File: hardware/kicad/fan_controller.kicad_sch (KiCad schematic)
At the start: 84 parts, among them J1 12V IN, J10 AIN2, J11 AIN3, J12 AIN4, J13 AIN5, J14 AIN6, J2 BluePill A, J3 BluePill B, J4 USB int, J5 FAN1, J6 FAN2, J7 FAN3, J8 FAN4, J9 AIN1, Q1 BSS138, Q2 BSS138, Q3 BSS138, Q4 BSS138, U1 USBLC6-2SC6

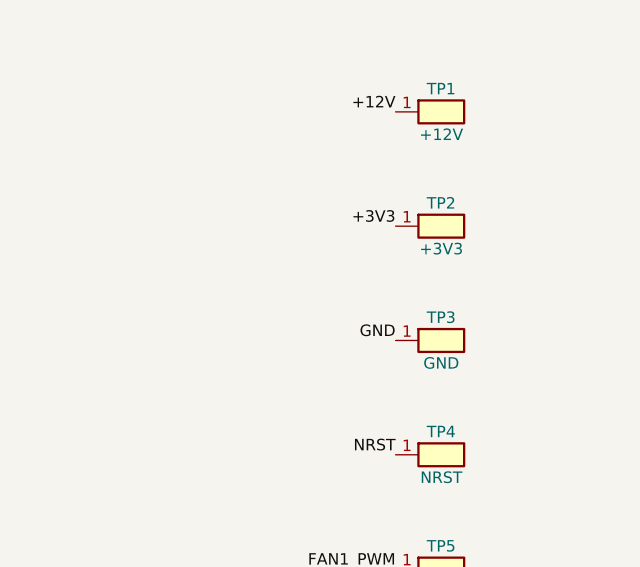
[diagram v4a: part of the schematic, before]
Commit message: hw: route 21 missing nets, remove 3V3/GND test point pair
21 nets (mostly BluePill header J2/J3 to main-board parts) were
never actually routed, despite earlier DRC checks reporting zero
errors - the MCP DRC wrapper used doesn't run KiCad's unconnected-
items check. Verified with native kicad-cli --severity-all.

Routed via Freerouting (autoroute, best-of-3), then manually closed
the 2 nets it couldn't finish (GND, +3V3A) and fixed a short the
autorouted +3V3A trace made against an existing GND track, plus a
board-edge clearance violation on FAN3_TACH.

Also removed TP2 (+3V3) / TP3 (GND), a probe pair that served no
circuit function, plus their stub traces.

Native kicad-cli DRC (10.0.7): 0 errors, 0 unconnected items.

Signed-off-by: Roman Skakun <rm.skakun@gmail.com>
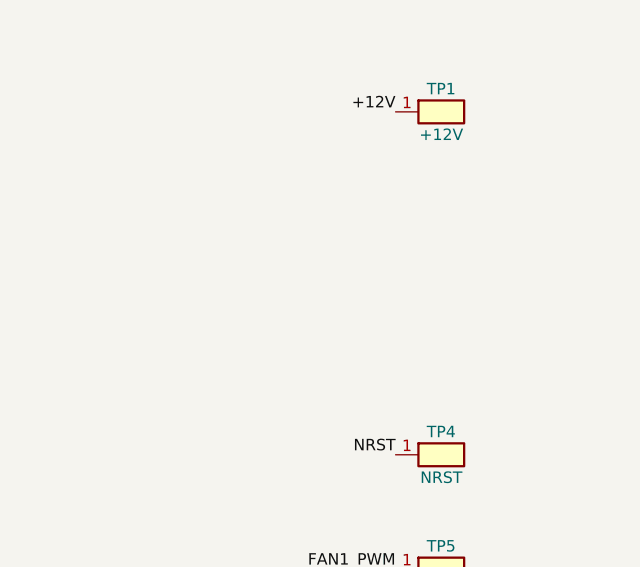
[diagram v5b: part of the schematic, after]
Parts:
- removed TP2: +3V3, TestPoint:TestPoint_Pad_D1.5mm, symbol fanctl:TestPoint
- removed TP3: GND, TestPoint:TestPoint_Pad_D1.5mm, symbol fanctl:TestPoint
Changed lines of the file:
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@@
 		)
 	)
-	(label "+3V3"
-		(at 736.6 58.42 180)
-		(effects
-			(font
-				(size 1.27 1.27)
-			)
-			(justify right bottom)
-		)
-	)
 	(label "GND"
 		(at 200.66 54.61 180)
@@
 		)
 	)
-	(label "GND"
-		(at 736.6 71.12 180)
-		(effects
-			(font
-				(size 1.27 1.27)
-			)
-			(justify right bottom)
-		)
-	)
 	(label "+5V"
 		(at 109.22 148.59 180)
@@
 	)
 	(symbol
-		(lib_id "fanctl:TestPoint")
-		(at 741.68 71.12 0)
-		(unit 1)
-		(body_style 1)
-		(exclude_from_sim no)
-		(in_bom yes)
-		(on_board yes)
-		(in_pos_files yes)
-		(dnp no)
-		(property "Reference" "TP3"
-			(at 741.68 68.58 0)
-			(show_name no)
-			(do_not_autoplace no)
-			(effects
-				(font
-					(size 1.27 1.27)
-				)
-			)
-		)
-		(property "Value" "GND"
-			(at 741.68 73.66 0)
-			(show_name no)
-			(do_not_autoplace no)
-			(effects
-				(font
-					(size 1.27 1.27)
-				)
-			)
-		)
-		(property "Footprint" "TestPoint:TestPoint_Pad_D1.5mm"
-			(at 741.68 71.12 0)
-			(hide yes)
-			(show_name no)
-			(do_not_autoplace no)
-			(effects
-				(font
-					(size 1.27 1.27)
-				)
-			)
-		)
-		(property "Datasheet" ""
-			(at 741.68 71.12 0)
-			(hide yes)
-			(show_name no)
-			(do_not_autoplace no)
-			(effects
-				(font
-					(size 1.27 1.27)
-				)
-			)
-		)
-		(property "Description" "Probe pad"
-			(at 741.68 71.12 0)
-			(hide yes)
-			(show_name no)
-			(do_not_autoplace no)
-			(effects
-				(font
-					(size 1.27 1.27)
-				)
-			)
-		)
-		(property "MPN" ""
-			(at 741.68 71.12 0)
-			(hide yes)
-			(show_name no)
-			(do_not_autoplace no)
-			(effects
-				(font
-					(size 1.27 1.27)
-				)
-			)
-		)
-		(pin "1"
-		)
-		(instances
-			(project "fan_controller"
-				(path "/70b8c4ee-a575-5d0b-ad3b-d6e1fd85f7ba"
-					(reference "TP3")
-					(unit 1)
-				)
-			)
-		)
-	)
-	(symbol
 		(lib_id "fanctl:Polyfuse")
 		(at 30.48 60.96 0)
@@
 					(unit 1)
 				)
-			)
-		)
-	)
-	(symbol
-		(lib_id "fanctl:TestPoint")
-		(at 741.68 58.42 0)
-		(unit 1)
-		(body_style 1)
-		(exclude_from_sim no)
-		(in_bom yes)
-		(on_board yes)
-		(in_pos_files yes)
-		(dnp no)
-		(property "Reference" "TP2"
-			(at 741.68 55.88 0)
-			(show_name no)
-			(do_not_autoplace no)
-			(effects
-				(font
-					(size 1.27 1.27)
-				)
-			)
-		)
-		(property "Value" "+3V3"
-			(at 741.68 60.96 0)
-			(show_name no)
-			(do_not_autoplace no)
-			(effects
-				(font
-					(size 1.27 1.27)
-				)
-			)
-		)
-		(property "Footprint" "TestPoint:TestPoint_Pad_D1.5mm"
-			(at 741.68 58.42 0)
-			(hide yes)
-			(show_name no)
-			(do_not_autoplace no)
-			(effects
-				(font
-					(size 1.27 1.27)
-				)
-			)
-		)
-		(property "Datasheet" ""
-			(at 741.68 58.42 0)
-			(hide yes)
-			(show_name no)
-			(do_not_autoplace no)
-			(effects
-				(font
-					(size 1.27 1.27)
-				)
-			)
-		)
-		(property "Description" "Probe pad"
-			(at 741.68 58.42 0)
-			(hide yes)
-			(show_name no)
-			(do_not_autoplace no)
-			(effects
-				(font
-					(size 1.27 1.27)
-				)
-			)
-		)
-		(property "MPN" ""
-			(at 741.68 58.42 0)
-			(hide yes)
-			(show_name no)
-			(do_not_autoplace no)
-			(effects
-				(font
-					(size 1.27 1.27)
-				)
-			)
-		)
-		(pin "1"
-		)
-		(instances
-			(project "fan_controller"
-				(path "/70b8c4ee-a575-5d0b-ad3b-d6e1fd85f7ba"
-					(reference "TP2")
-					(unit 1)
-				)

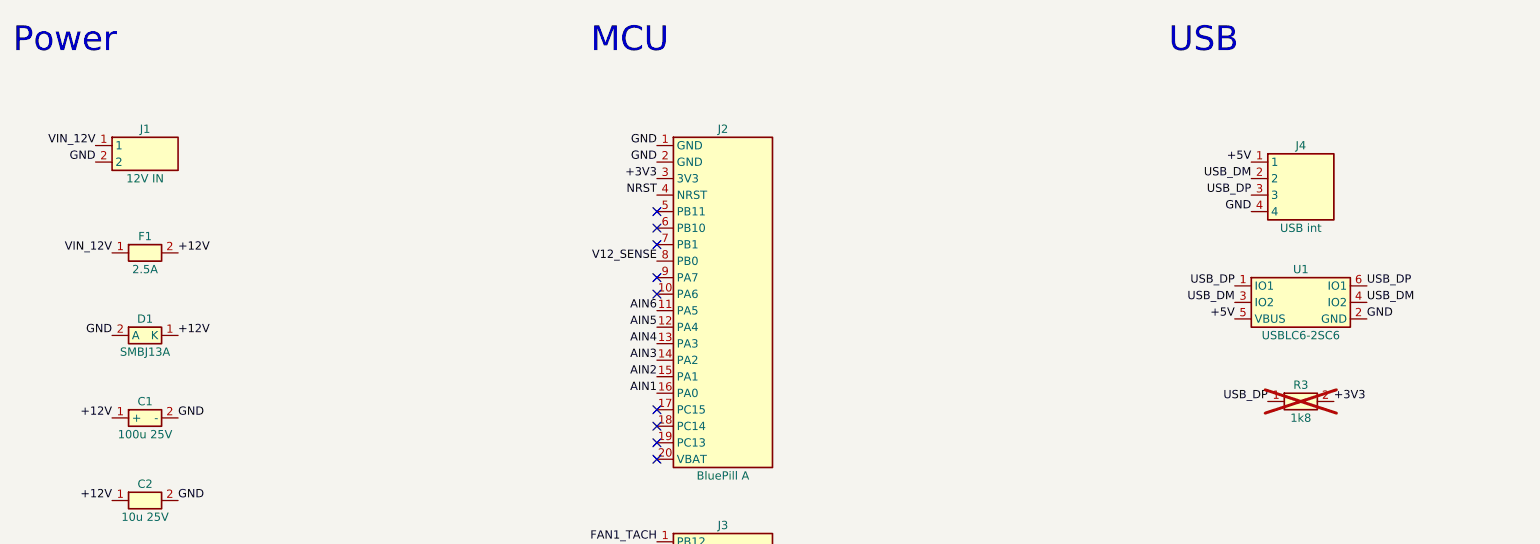
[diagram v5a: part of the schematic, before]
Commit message: hw: swap 12V connector to Mate-N-Lok, drop main-board USB, rotate J3
Replace J1 (2-pin Phoenix screw terminal) with TE Connectivity
350424-1, a 4-circuit Mate-N-Lok PCB header (2x GND + 2x VIN_12V,
12A/250V per pin, 0.2in pitch). Custom footprint built from the
part's real datasheet drawing (drill/pitch), registered as a
project-local fanctl.pretty library since no footprint libraries
are installed in this environment.

Remove the main-board USB path entirely (J4 header, U1 ESD chip,
R3 pullup): the Blue Pill module's own USB port covers this, so
routing USB_DP/USB_DM across the main board was unnecessary. This
also freed board area.

Rotate J3 (Blue Pill B header) 180 degrees in place, and relocate
the 12V input protection cluster (F1 fuse, D1 TVS, C1 bulk cap,
C2 10u cap, FB1 ferrite) into the space freed by the USB removal,
to fit the physically larger J1 connector without colliding with
J3's courtyard.

KNOWN INCOMPLETE: native kicad-cli --severity-all DRC currently
reports 5 unconnected items, 7 shorts, and 3 track crossings,
all localized to the relocated F1/D1/C1/C2/FB1 cluster and nearby
NRST routing. Needs one more Freerouting pass on +12V/GND/NRST/
+3V3A plus manual cleanup before this is fab-ready. gen_kicad.py
(the board's generator script / BOM source of truth) has not yet
been updated to match these changes.

Signed-off-by: Roman Skakun <rm.skakun@gmail.com>
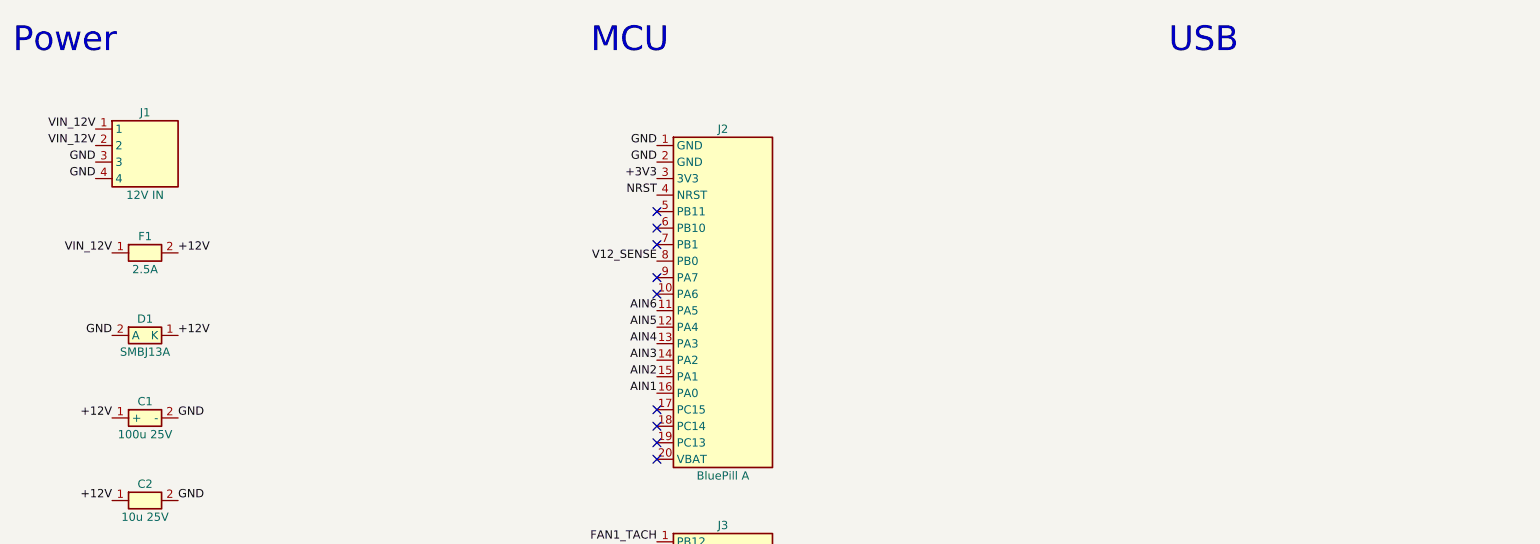
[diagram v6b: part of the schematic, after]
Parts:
- removed J1: 12V IN, TerminalBlock_Phoenix:TerminalBlock_Phoenix_MKDS-1,5-2-5.08_1x02_P5.08mm_Horizontal, symbol fanctl:Conn_01x02
- removed J4: USB int, Connector_PinHeader_2.54mm:PinHeader_1x04_P2.54mm_Vertical, symbol fanctl:Conn_01x04
- removed R3: 1k8, Resistor_SMD:R_0603_1608Metric, symbol fanctl:R
- removed U1: USBLC6-2SC6, Package_TO_SOT_SMD:SOT-23-6, symbol fanctl:USBLC6-2SC6
- added J1: 12V IN, fanctl:ConnHeader_MateNLok_1x04_P5.08mm_Vertical, symbol fanctl:Conn_01x04
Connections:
- net GND: now also J1.3, J1.4
- net VIN_12V: now also J1.1, J1.2

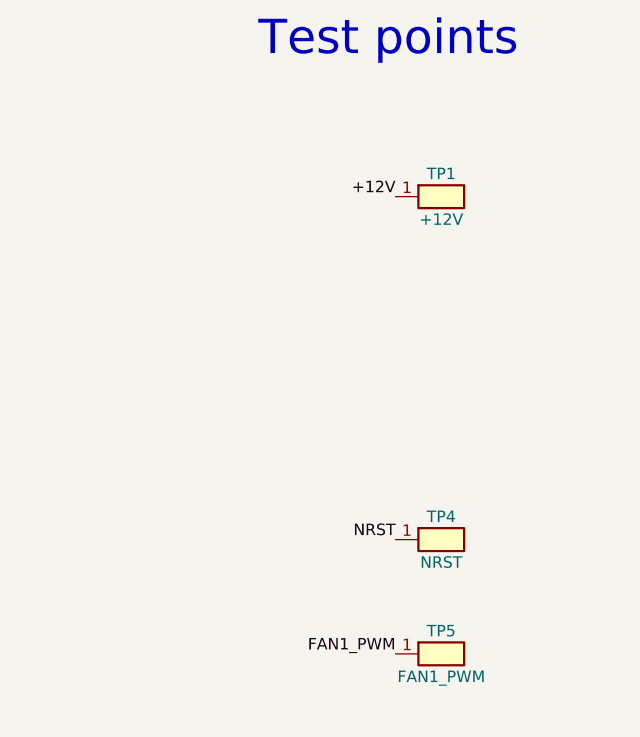
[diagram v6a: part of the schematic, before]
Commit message: hw: sync schematic to board after removing TP1/TP4 test points
Board no longer carries TP1 (+12V probe) and TP4 (NRST probe); remove
the matching symbols and their orphaned net labels from the schematic
so both files agree. Cross-checked all 77 references: footprints and
values now match exactly between schematic and board.

ERC: 0 errors, 4 warnings (pre-existing single-pin-label style,
consistent with the rest of the sheet).

Signed-off-by: Roman Skakun <rm.skakun@gmail.com>
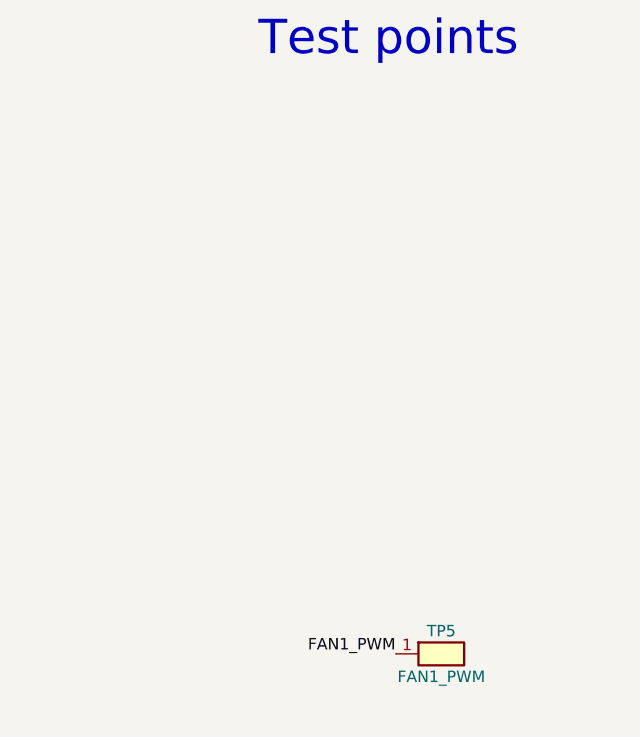
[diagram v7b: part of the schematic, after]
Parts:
- removed TP1: +12V, TestPoint:TestPoint_Pad_D1.5mm, symbol fanctl:TestPoint
- removed TP4: NRST, TestPoint:TestPoint_Pad_D1.5mm, symbol fanctl:TestPoint
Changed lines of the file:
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@@
 		)
 	)
-	(label "NRST"
-		(at 736.6 83.82 180)
-		(effects
-			(font
-				(size 1.27 1.27)
-			)
-			(justify right bottom)
-		)
-	)
 	(label "AIN2_IN"
 		(at 647.7 149.86 180)
@@
 		)
 	)
-	(label "+12V"
-		(at 736.6 45.72 180)
-		(effects
-			(font
-				(size 1.27 1.27)
-			)
-			(justify right bottom)
-		)
-	)
 	(label "FAN4_TACH_IN"
 		(at 558.8 114.3 180)
@@
 	)
 	(symbol
-		(lib_id "fanctl:TestPoint")
-		(at 741.68 83.82 0)
-		(unit 1)
-		(body_style 1)
-		(exclude_from_sim no)
-		(in_bom yes)
-		(on_board yes)
-		(in_pos_files yes)
-		(dnp no)
-		(property "Reference" "TP4"
-			(at 741.68 81.28 0)
-			(show_name no)
-			(do_not_autoplace no)
-			(effects
-				(font
-					(size 1.27 1.27)
-				)
-			)
-		)
-		(property "Value" "NRST"
-			(at 741.68 86.36 0)
-			(show_name no)
-			(do_not_autoplace no)
-			(effects
-				(font
-					(size 1.27 1.27)
-				)
-			)
-		)
-		(property "Footprint" "TestPoint:TestPoint_Pad_D1.5mm"
-			(at 741.68 83.82 0)
-			(hide yes)
-			(show_name no)
-			(do_not_autoplace no)
-			(effects
-				(font
-					(size 1.27 1.27)
-				)
-			)
-		)
-		(property "Datasheet" ""
-			(at 741.68 83.82 0)
-			(hide yes)
-			(show_name no)
-			(do_not_autoplace no)
-			(effects
-				(font
-					(size 1.27 1.27)
-				)
-			)
-		)
-		(property "Description" "Probe pad"
-			(at 741.68 83.82 0)
-			(hide yes)
-			(show_name no)
-			(do_not_autoplace no)
-			(effects
-				(font
-					(size 1.27 1.27)
-				)
-			)
-		)
-		(property "MPN" ""
-			(at 741.68 83.82 0)
-			(hide yes)
-			(show_name no)
-			(do_not_autoplace no)
-			(effects
-				(font
-					(size 1.27 1.27)
-				)
-			)
-		)
-		(pin "1"
-		)
-		(instances
-			(project "fan_controller"
-				(path "/70b8c4ee-a575-5d0b-ad3b-d6e1fd85f7ba"
-					(reference "TP4")
-					(unit 1)
-				)
-			)
-		)
-	)
-	(symbol
 		(lib_id "fanctl:BAT54S")
 		(at 652.78 462.28 0)
@@
 					(unit 1)
 				)
-			)
-		)
-	)
-	(symbol
-		(lib_id "fanctl:TestPoint")
-		(at 741.68 45.72 0)
-		(unit 1)
-		(body_style 1)
-		(exclude_from_sim no)
-		(in_bom yes)
-		(on_board yes)
-		(in_pos_files yes)
-		(dnp no)
-		(property "Reference" "TP1"
-			(at 741.68 43.18 0)
-			(show_name no)
-			(do_not_autoplace no)
-			(effects
-				(font
-					(size 1.27 1.27)
-				)
-			)
-		)
-		(property "Value" "+12V"
-			(at 741.68 48.26 0)
-			(show_name no)
-			(do_not_autoplace no)
-			(effects
-				(font
-					(size 1.27 1.27)
-				)
-			)
-		)
-		(property "Footprint" "TestPoint:TestPoint_Pad_D1.5mm"
-			(at 741.68 45.72 0)
-			(hide yes)
-			(show_name no)
-			(do_not_autoplace no)
-			(effects
-				(font
-					(size 1.27 1.27)
-				)
-			)
-		)
-		(property "Datasheet" ""
-			(at 741.68 45.72 0)
-			(hide yes)
-			(show_name no)
-			(do_not_autoplace no)
-			(effects
-				(font
-					(size 1.27 1.27)
-				)
-			)
-		)
-		(property "Description" "Probe pad"
-			(at 741.68 45.72 0)
-			(hide yes)
-			(show_name no)
-			(do_not_autoplace no)
-			(effects
-				(font
-					(size 1.27 1.27)
-				)
-			)
-		)
-		(property "MPN" ""
-			(at 741.68 45.72 0)
-			(hide yes)
-			(show_name no)
-			(do_not_autoplace no)
-			(effects
-				(font
-					(size 1.27 1.27)
-				)
-			)
-		)
-		(pin "1"
-		)
-		(instances
-			(project "fan_controller"
-				(path "/70b8c4ee-a575-5d0b-ad3b-d6e1fd85f7ba"
-					(reference "TP1")
-					(unit 1)
-				)

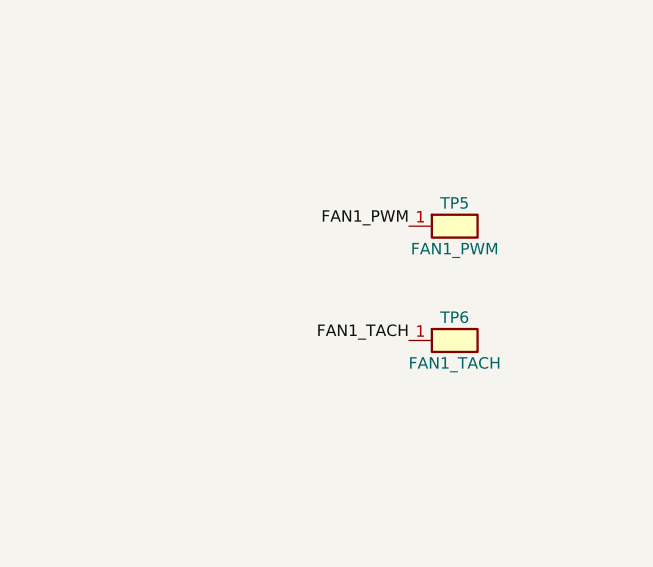
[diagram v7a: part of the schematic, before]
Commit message: hw: sync schematic to board after removing TP5/TP6, regen render
Board no longer carries TP5 (FAN1_PWM probe) and TP6 (FAN1_TACH
probe); remove the matching symbols and their orphaned net labels
from the schematic so both files agree. Cross-checked all 75
references: footprints match exactly between schematic and board.

ERC: 0 errors, 4 warnings (pre-existing single-pin-label style).
Regenerated hardware/pcb_3d.png at current board state.

Signed-off-by: Roman Skakun <rm.skakun@gmail.com>
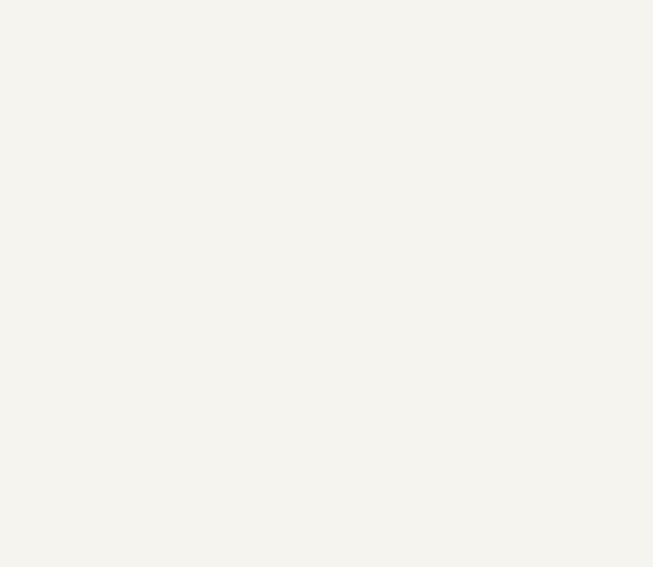
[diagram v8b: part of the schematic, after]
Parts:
- removed TP5: FAN1_PWM, TestPoint:TestPoint_Pad_D1.5mm, symbol fanctl:TestPoint
- removed TP6: FAN1_TACH, TestPoint:TestPoint_Pad_D1.5mm, symbol fanctl:TestPoint
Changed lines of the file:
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@@
 		)
 	)
-	(label "FAN1_TACH"
-		(at 736.6 109.22 180)
-		(effects
-			(font
-				(size 1.27 1.27)
-			)
-			(justify right bottom)
-		)
-	)
 	(label "FAN4_PWM_G"
 		(at 556.26 59.69 180)
@@
 		)
 	)
-	(label "FAN1_PWM"
-		(at 736.6 96.52 180)
-		(effects
-			(font
-				(size 1.27 1.27)
-			)
-			(justify right bottom)
-		)
-	)
 	(label "FAN3_PWM_G"
 		(at 467.36 59.69 180)
@@
 	)
 	(symbol
-		(lib_id "fanctl:TestPoint")
-		(at 741.68 96.52 0)
-		(unit 1)
-		(body_style 1)
-		(exclude_from_sim no)
-		(in_bom yes)
-		(on_board yes)
-		(in_pos_files yes)
-		(dnp no)
-		(property "Reference" "TP5"
-			(at 741.68 93.98 0)
-			(show_name no)
-			(do_not_autoplace no)
-			(effects
-				(font
-					(size 1.27 1.27)
-				)
-			)
-		)
-		(property "Value" "FAN1_PWM"
-			(at 741.68 99.06 0)
-			(show_name no)
-			(do_not_autoplace no)
-			(effects
-				(font
-					(size 1.27 1.27)
-				)
-			)
-		)
-		(property "Footprint" "TestPoint:TestPoint_Pad_D1.5mm"
-			(at 741.68 96.52 0)
-			(hide yes)
-			(show_name no)
-			(do_not_autoplace no)
-			(effects
-				(font
-					(size 1.27 1.27)
-				)
-			)
-		)
-		(property "Datasheet" ""
-			(at 741.68 96.52 0)
-			(hide yes)
-			(show_name no)
-			(do_not_autoplace no)
-			(effects
-				(font
-					(size 1.27 1.27)
-				)
-			)
-		)
-		(property "Description" "Probe pad"
-			(at 741.68 96.52 0)
-			(hide yes)
-			(show_name no)
-			(do_not_autoplace no)
-			(effects
-				(font
-					(size 1.27 1.27)
-				)
-			)
-		)
-		(property "MPN" ""
-			(at 741.68 96.52 0)
-			(hide yes)
-			(show_name no)
-			(do_not_autoplace no)
-			(effects
-				(font
-					(size 1.27 1.27)
-				)
-			)
-		)
-		(pin "1"
-		)
-		(instances
-			(project "fan_controller"
-				(path "/70b8c4ee-a575-5d0b-ad3b-d6e1fd85f7ba"
-					(reference "TP5")
-					(unit 1)
-				)
-			)
-		)
-	)
-	(symbol
 		(lib_id "fanctl:R")
 		(at 386.08 114.3 0)
@@
 					(unit 1)
 				)
-			)
-		)
-	)
-	(symbol
-		(lib_id "fanctl:TestPoint")
-		(at 741.68 109.22 0)
-		(unit 1)
-		(body_style 1)
-		(exclude_from_sim no)
-		(in_bom yes)
-		(on_board yes)
-		(in_pos_files yes)
-		(dnp no)
-		(property "Reference" "TP6"
-			(at 741.68 106.68 0)
-			(show_name no)
-			(do_not_autoplace no)
-			(effects
-				(font
-					(size 1.27 1.27)
-				)
-			)
-		)
-		(property "Value" "FAN1_TACH"
-			(at 741.68 111.76 0)
-			(show_name no)
-			(do_not_autoplace no)
-			(effects
-				(font
-					(size 1.27 1.27)
-				)
-			)
-		)
-		(property "Footprint" "TestPoint:TestPoint_Pad_D1.5mm"
-			(at 741.68 109.22 0)
-			(hide yes)
-			(show_name no)
-			(do_not_autoplace no)
-			(effects
-				(font
-					(size 1.27 1.27)
-				)
-			)
-		)
-		(property "Datasheet" ""
-			(at 741.68 109.22 0)
-			(hide yes)
-			(show_name no)
-			(do_not_autoplace no)
-			(effects
-				(font
-					(size 1.27 1.27)
-				)
-			)
-		)
-		(property "Description" "Probe pad"
-			(at 741.68 109.22 0)
-			(hide yes)
-			(show_name no)
-			(do_not_autoplace no)
-			(effects
-				(font
-					(size 1.27 1.27)
-				)
-			)
-		)
-		(property "MPN" ""
-			(at 741.68 109.22 0)
-			(hide yes)
-			(show_name no)
-			(do_not_autoplace no)
-			(effects
-				(font
-					(size 1.27 1.27)
-				)
-			)
-		)
-		(pin "1"
-		)
-		(instances
-			(project "fan_controller"
-				(path "/70b8c4ee-a575-5d0b-ad3b-d6e1fd85f7ba"
-					(reference "TP6")
-					(unit 1)
-				)
